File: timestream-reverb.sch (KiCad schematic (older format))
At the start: 42 parts

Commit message: Annotate
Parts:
- gave numbers to parts that had none: 38

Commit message: Finish PCB
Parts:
- added J1, J2, J3, J4, J5: Conn_01x01_Female, Connector_Wire:SolderWire-0.1sqmm_1x01_D0.4mm_OD1mm, symbol Connector:Conn_01x01_Female
- C1, C2, C3, C4, C5, C7: footprint (none) -> Capacitor_THT:CP_Radial_D5.0mm_P2.00mm
- C10: footprint (none) -> Capacitor_THT:C_Disc_D3.0mm_W1.6mm_P2.50mm
- C11, C12, C6, C8, C9: footprint (none) -> Capacitor_THT:C_Rect_L7.0mm_W2.5mm_P5.00mm
- D1: footprint (none) -> LED_THT:LED_D5.0mm
- D2: footprint (none) -> Diode_THT:D_DO-41_SOD81_P7.62mm_Horizontal
- R1, R10, R11, R12, R13, R14, R15, R2, R3, R4, R5, R6, R7, R8, R9: footprint (none) -> Resistor_THT:R_Axial_DIN0207_L6.3mm_D2.5mm_P10.16mm_Horizontal
- RV1, RV2, RV3, RV4: footprint (none) -> Potentiometer_THT:Potentiometer_Omeg_PC16BU_Vertical
- SW1: footprint (none) -> Connector_Wire:SolderWire-0.1sqmm_1x03_P3.6mm_D0.4mm_OD1mm
- U2, U3: footprint (none) -> Package_DIP:DIP-8_W7.62mm
- U4: footprint (none) -> timestream-reverb:BTDR-2H
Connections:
- net +9V: now also J3.1 (Pin_1)
- net FS: now also J4.1 (Pin_1)
- net GND: now also J5.1 (Pin_1)
- net IN: now also J1.1 (Pin_1)
- net OUT: now also J2.1 (Pin_1)
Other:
- moved on the sheet: C1, C10, C11, C12, C2, C3, C4, C5, C6, C7, C8, C9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

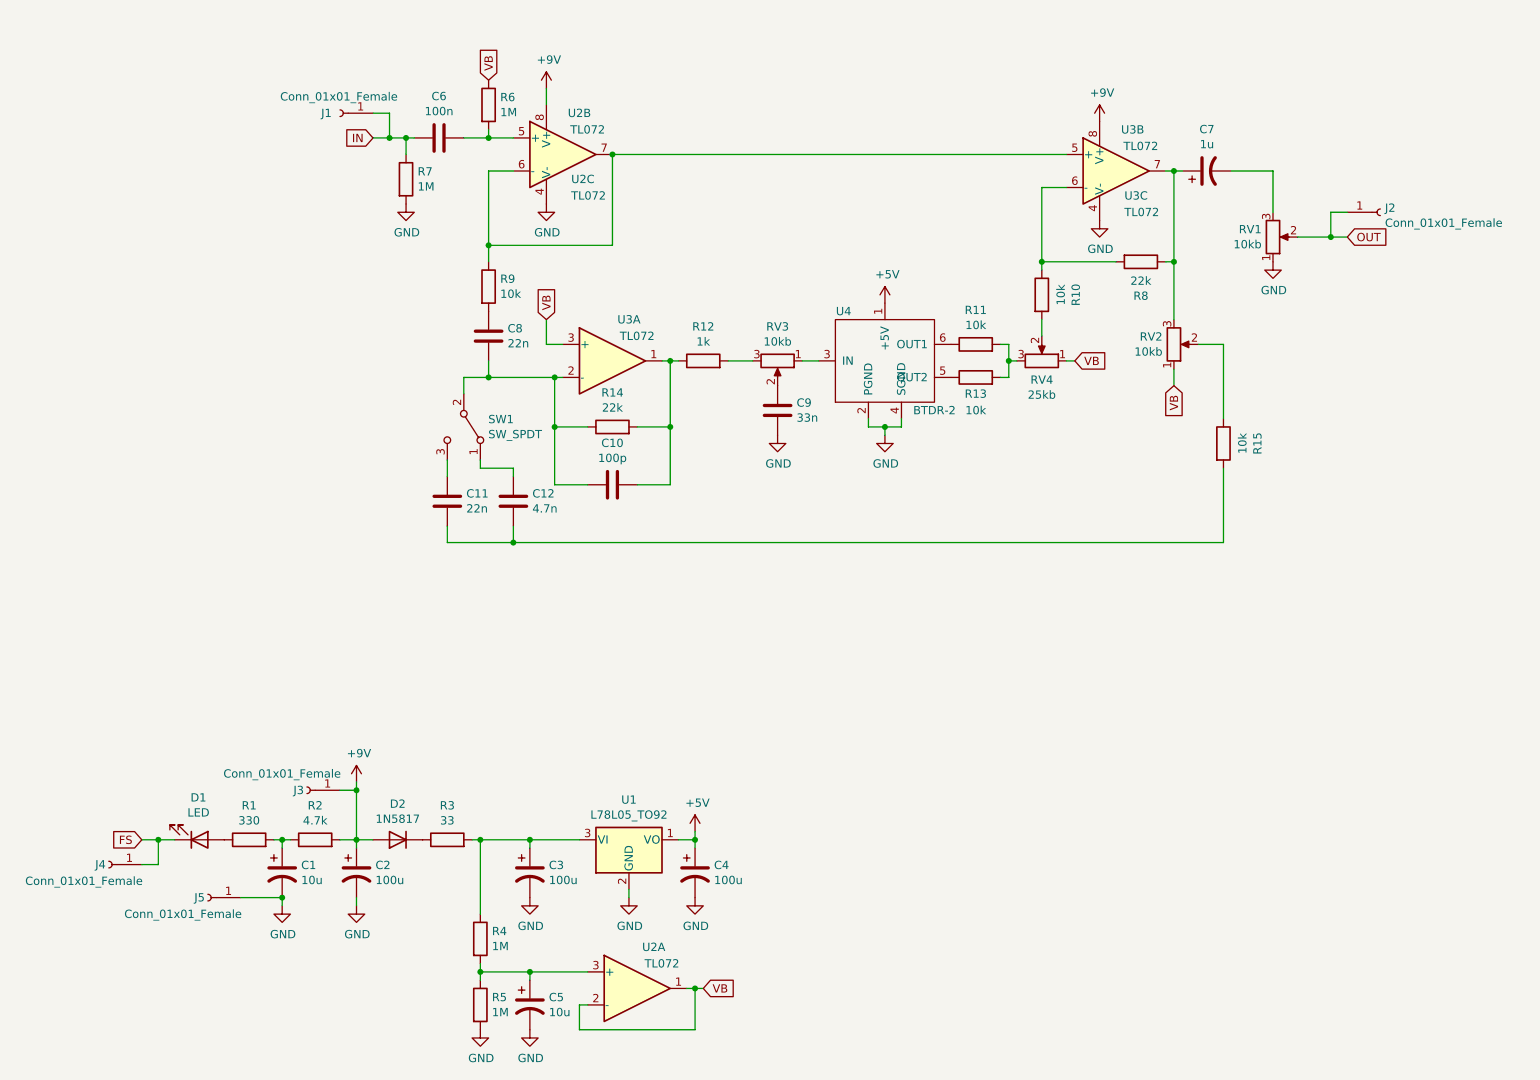
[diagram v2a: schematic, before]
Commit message: fix: Improve layout and remove wires to PCB
The following has been fixed:
  - Wires are no longer wired to the PCB
  - PCB size is smaller
  - LED is not included in the layout
  - BTDR-2 is not included in the layout
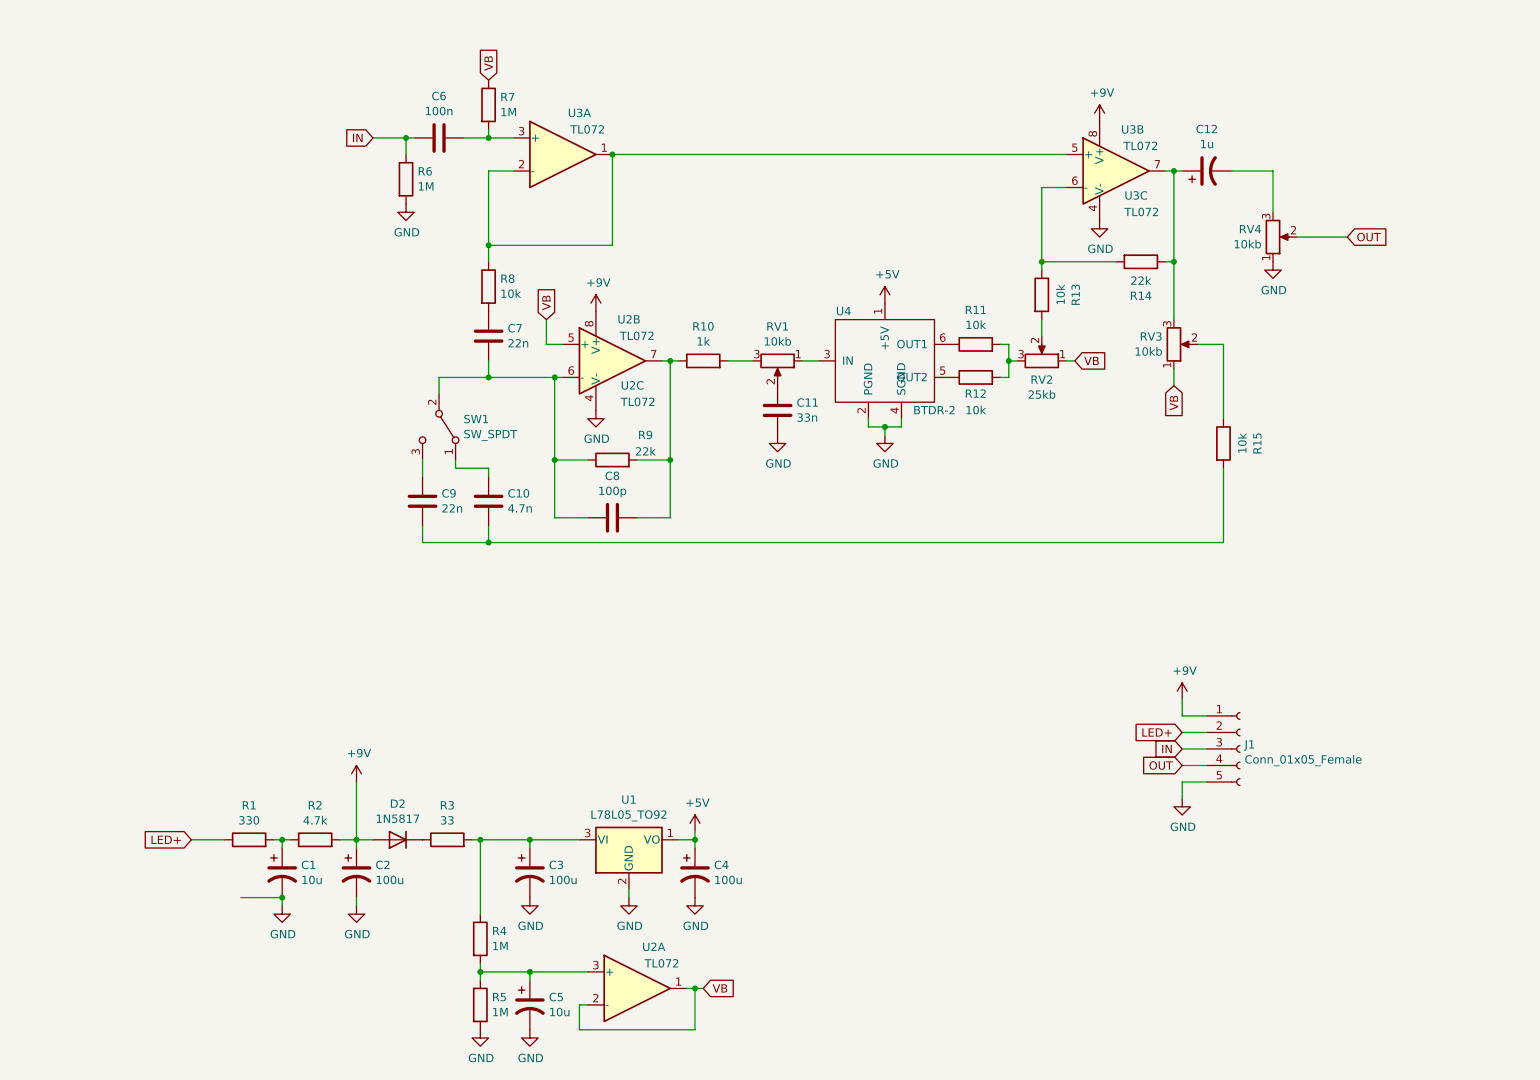
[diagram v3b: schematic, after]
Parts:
- removed D1: LED, LED_THT:LED_D5.0mm, symbol Device:LED
- removed J1, J2, J3, J4, J5: Conn_01x01_Female, Connector_Wire:SolderWire-0.1sqmm_1x01_D0.4mm_OD1mm, symbol Connector:Conn_01x01_Female
- added J1: Conn_01x05_Female, timestream-reverb:TerminalBlock_5pin_2.54mm, symbol Connector:Conn_01x05_Female
- RV1: renamed from RV3; footprint Potentiometer_THT:Potentiometer_Omeg_PC16BU_Vertical -> timestream-reverb:Tayda_Potentiometer
- RV2: renamed from RV4; footprint Potentiometer_THT:Potentiometer_Omeg_PC16BU_Vertical -> timestream-reverb:Tayda_Potentiometer
- RV3: renamed from RV2; footprint Potentiometer_THT:Potentiometer_Omeg_PC16BU_Vertical -> timestream-reverb:Tayda_Potentiometer
- RV4: renamed from RV1; footprint Potentiometer_THT:Potentiometer_Omeg_PC16BU_Vertical -> timestream-reverb:Tayda_Potentiometer
- SW1: footprint Connector_Wire:SolderWire-0.1sqmm_1x03_P3.6mm_D0.4mm_OD1mm -> timestream-reverb:TerminalBlock_3pin_2.54mm
- U4: footprint timestream-reverb:BTDR-2H -> timestream-reverb:TerminalBlock_6pin_2.54mm
- renumbered C12 to C10, C9 to C11, C7 to C12, C8 to C7, C10 to C8, C11 to C9, R12 to R10, R13 to R12, R10 to R13, R8 to R14, R7 to R6, R6 to R7, R9 to R8, R14 to R9
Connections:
- net +9V: now also J1.1 (Pin_1)
- net GND: now also J1.5 (Pin_5)
- net IN: now also J1.3 (Pin_3)
- net OUT: now also J1.4 (Pin_4)
- net VB: now also U2.5 (+); no longer U3.3 (+)
- net LED+: now reaches R1.1
- net LED+: now also J1.2 (Pin_2)
- net at C6.1, R7.2: now also U3.3 (+); no longer U2.5 (+)
- net at R8.1, U3.5 (+): now also U3.1, U3.2 (-); no longer U2.6 (-), U2.7
- net at C7.1, C8.1, R9.1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: now also U2.6 (-); no longer U3.2 (-)
- net at C8.2, R10.1, R9.2: now also U2.7; no longer U3.1
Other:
- moved on the sheet: C10, C8, C9, R9, SW1, U2B, U2C, U3A
